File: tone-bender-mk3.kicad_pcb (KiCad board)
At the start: 4 copper layers, 56 x 60 mm, 41 parts, among them P1 IN, P2 GND, P3 -9V, P6 GND, P7 OUT, P8 GND, Q1 PNP_Ge, Q2 PNP_Ge, Q3 PNP_Ge

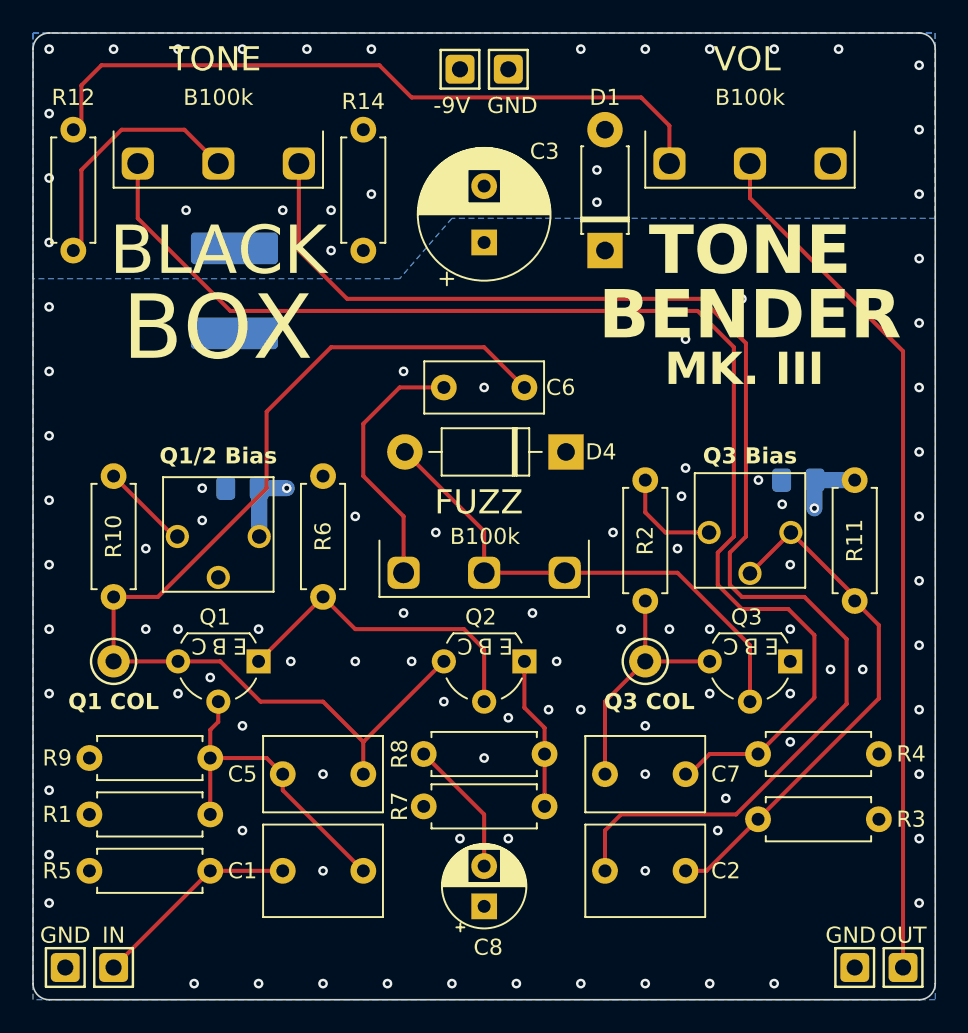
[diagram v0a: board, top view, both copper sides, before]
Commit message: Added gnd pour to top layer
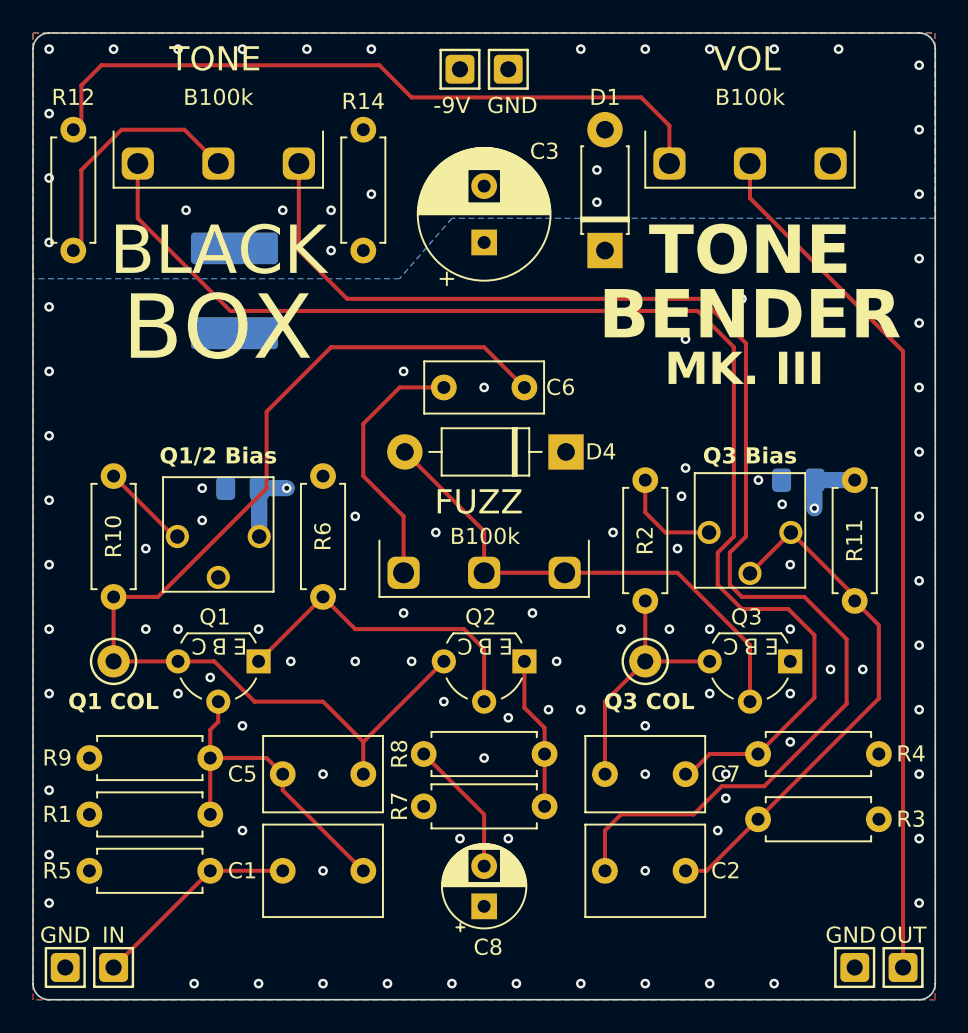
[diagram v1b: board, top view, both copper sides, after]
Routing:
- net GND: vias 101 -> 102
- added copper zone on F.Cu, net GND
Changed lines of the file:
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@@
+	)
+	(segment
+		(start 105.5 122.638299)
+		(end 100.388299 127.75)
+		(width 0.25)
+		(layer "F.Cu")
+		(net 4)
+	)
+	(segment
+		(start 98.25 113.25)
+		(end 98.25 115.25)
+		(width 0.25)
+		(layer "F.Cu")
+		(net 4)
+	)
+	(segment
+		(start 96 129.5)
+		(end 91.5 129.5)
+		(width 0.25)
+		(layer "F.Cu")
+		(net 4)
+	)
+	(segment
+		(start 71.5 89.1)
+		(end 71.5 94.5)
+		(width 0.25)
+		(layer "F.Cu")
+		(net 4)
+	)
+	(segment
+		(start 100.388299 127.75)
+		(end 97.75 127.75)
+		(width 0.25)
+		(layer "F.Cu")
+		(net 4)
+	)
+	(segment
+		(start 71.5 94.5)
+		(end 74.5 97.5)
+		(width 0.25)
+		(layer "F.Cu")
+		(net 4)
+	)
+	(segment
+		(start 98.25 115.25)
+		(end 99 116)
+		(width 0.25)
+		(layer "F.Cu")
+		(net 4)
+	)
+	(segment
+		(start 102.875 116)
+		(end 105.5 118.625)
+		(width 0.25)
+		(layer "F.Cu")
+		(net 4)
+	)
+	(segment
+		(start 105.5 118.625)
+		(end 105.5 122.638299)
+		(width 0.25)
+		(layer "F.Cu")
+		(net 4)
+	)
+	(segment
+		(start 91.5 129.5)
+		(end 90.5 130.5)
+		(width 0.25)
+		(layer "F.Cu")
+		(net 4)
+	)
+	(segment
+		(start 99.25 100.25)
+		(end 99.25 112.25)
+		(width 0.25)
+		(layer "F.Cu")
+		(net 4)
 	)
 	(segment
@@
 	)
 	(segment
-		(start 98.25 113.25)
-		(end 98.25 115.25)
-		(width 0.25)
-		(layer "F.Cu")
-		(net 4)
-	)
-	(segment
 		(start 90.5 130.5)
 		(end 90.5 133)
@@
 	)
 	(segment
-		(start 98.25 115.25)
-		(end 99 116)
+		(start 97.75 127.75)
+		(end 96 129.5)
 		(width 0.25)
 		(layer "F.Cu")
@@
 	)
 	(segment
-		(start 105.5 122.638299)
-		(end 98.638299 129.5)
-		(width 0.25)
-		(layer "F.Cu")
-		(net 4)
-	)
-	(segment
-		(start 105.5 118.625)
-		(end 105.5 122.638299)
-		(width 0.25)
-		(layer "F.Cu")
-		(net 4)
-	)
-	(segment
-		(start 102.875 116)
-		(end 105.5 118.625)
-		(width 0.25)
-		(layer "F.Cu")
-		(net 4)
-	)
-	(segment
-		(start 98.638299 129.5)
-		(end 91.5 129.5)
-		(width 0.25)
-		(layer "F.Cu")
-		(net 4)
-	)
-	(segment
-		(start 91.5 129.5)
-		(end 90.5 130.5)
-		(width 0.25)
-		(layer "F.Cu")
-		(net 4)
-	)
-	(segment
-		(start 99.25 100.25)
-		(end 99.25 112.25)
-		(width 0.25)
-		(layer "F.Cu")
-		(net 4)
-	)
-	(segment
-		(start 71.5 89.1)
-		(end 71.5 94.5)
+		(start 74.5 97.5)
+		(end 96.5 97.5)
 		(width 0.25)
 		(layer "F.Cu")
@@
 		(start 96.5 97.5)
 		(end 99.25 100.25)
-		(width 0.25)
-		(layer "F.Cu")
-		(net 4)
-	)
-	(segment
-		(start 71.5 94.5)
-		(end 74.5 97.5)
-		(width 0.25)
-		(layer "F.Cu")
-		(net 4)
-	)
-	(segment
-		(start 74.5 97.5)
-		(end 96.5 97.5)
 		(width 0.25)
 		(layer "F.Cu")
@@
 	)
 	(via
+		(at 98 127)
+		(size 0.6)
+		(drill 0.3)
+		(layers "F.Cu" "B.Cu")
+		(free yes)
+		(net 6)
+	)
+	(via
 		(at 95 113)
 		(size 0.6)
@@
 		(free yes)
 		(net 6)
+	)
+	(segment
+		(start 64 120)
+		(end 66.25 120)
+		(width 0.25)
+		(layer "F.Cu")
+		(net 7)
+	)
+	(segment
+		(start 69.5 104.5)
+		(end 73.5 100.5)
+		(width 0.25)
+		(layer "F.Cu")
+		(net 7)
+	)
+	(segment
+		(start 75.5 125)
+		(end 80.5 120)
+		(width 0.25)
+		(layer "F.Cu")
+		(net 7)
+	)
+	(segment
+		(start 60 116)
+		(end 62.75 116)
+		(width 0.25)
+		(layer "F.Cu")
+		(net 7)
+	)
+	(segment
+		(start 73.5 100.5)
+		(end 83 100.5)
+		(width 0.25)
+		(layer "F.Cu")
+		(net 7)
 	)
 	(segment
@@
 	)
 	(segment
-		(start 69.5 104.5)
-		(end 73.5 100.5)
-		(width 0.25)
-		(layer "F.Cu")
-		(net 7)
-	)
-	(segment
-		(start 75.5 125)
-		(end 80.5 120)
-		(width 0.25)
-		(layer "F.Cu")
-		(net 7)
-	)
-	(segment
-		(start 60 116)
-		(end 62.75 116)
-		(width 0.25)
-		(layer "F.Cu")
-		(net 7)
-	)
-	(segment
-		(start 73.5 100.5)
-		(end 83 100.5)
-		(width 0.25)
-		(layer "F.Cu")
-		(net 7)
-	)
-	(segment
 		(start 75.5 127)
 		(end 75.5 125)
@@
 	)
 	(segment
-		(start 64 120)
-		(end 66.625 120)
-		(width 0.25)
-		(layer "F.Cu")
-		(net 7)
-	)
-	(segment
 		(start 69.5 109.25)
 		(end 69.5 104.5)
@@
 	)
 	(segment
+		(start 66.25 120)
+		(end 68.75 122.5)
+		(width 0.25)
+		(layer "F.Cu")
+		(net 7)
+	)
+	(segment
 		(start 62.75 116)
 		(end 69.5 109.25)
@@
 	)
 	(segment
-		(start 66.625 120)
-		(end 69.125 122.5)
-		(width 0.25)
-		(layer "F.Cu")
-		(net 7)
-	)
-	(segment
-		(start 69.125 122.5)
-		(end 73 122.5)
-		(width 0.25)
-		(layer "F.Cu")
-		(net 7)
-	)
-	(segment
 		(start 64 120)
 		(end 60 120)
@@
 	)
 	(segment
+		(start 68.75 122.5)
+		(end 73 122.5)
+		(width 0.25)
+		(layer "F.Cu")
+		(net 7)
+	)
+	(segment
 		(start 77.75 103)
 		(end 80.5 103)
@@
 	)
 	(zone
+		(net 6)
+		(net_name "GND")
+		(layer "F.Cu")
+		(hatch edge 0.5)
+		(priority 4)
+		(connect_pads
+			(clearance 0.2)
+		)
+		(min_thickness 0.2)
+		(filled_areas_thickness no)
+		(fill yes
+			(thermal_gap 0.2)
+			(thermal_bridge_width 0.2)
+		)
+		(polygon
+			(pts
+				(xy 55 81) (xy 111 81) (xy 111 141) (xy 55 141)
+			)
+		)
+	)
+	(zone
